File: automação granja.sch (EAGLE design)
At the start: 76 parts, among them IC1 MEGA8-P, IC10 A1322UA, IC11 A1322UA, IC12 A1322UA, IC2 MAX481CPA, IC3 A1322UA, IC4 A1322UA, IC5 78L05Z, IC7 A1322UA, IC8 A1322UA, IC9 A1322UA, K1 G2RA, K2 G2RA, K3 G2RA, K4 G2RA, K5 G2RA, K6 G2RA, K7 G2RA, K8 G2RA, Q1 BC548B, Q2 BC548B, Q3 BC548B, Q4 BC548B, Q6 BC548B, Q7 BC548B, Q8 BC548B, Q9 BC548B

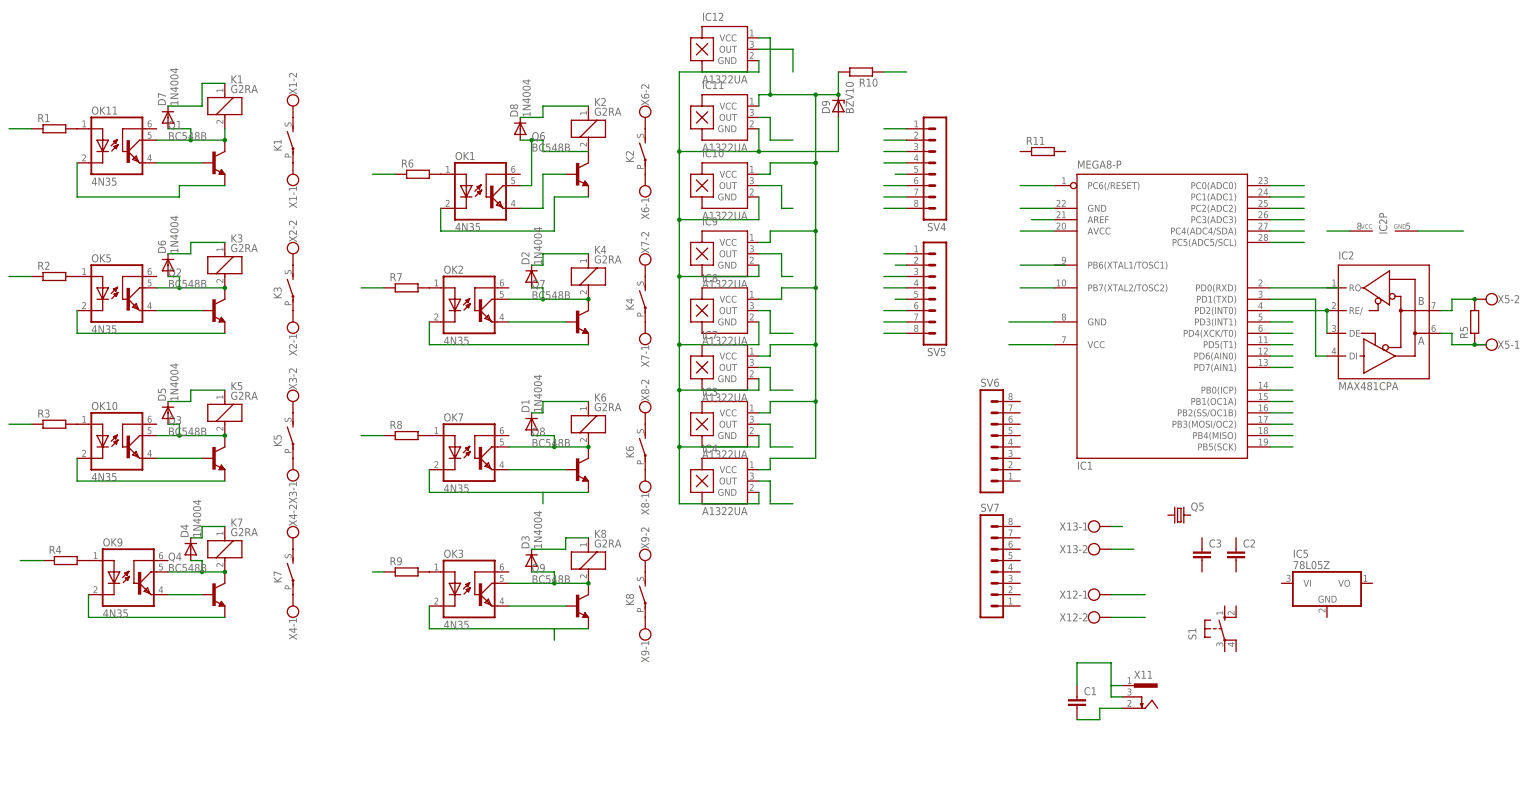
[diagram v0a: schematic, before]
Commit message: separadas controle de atuação e realimentação
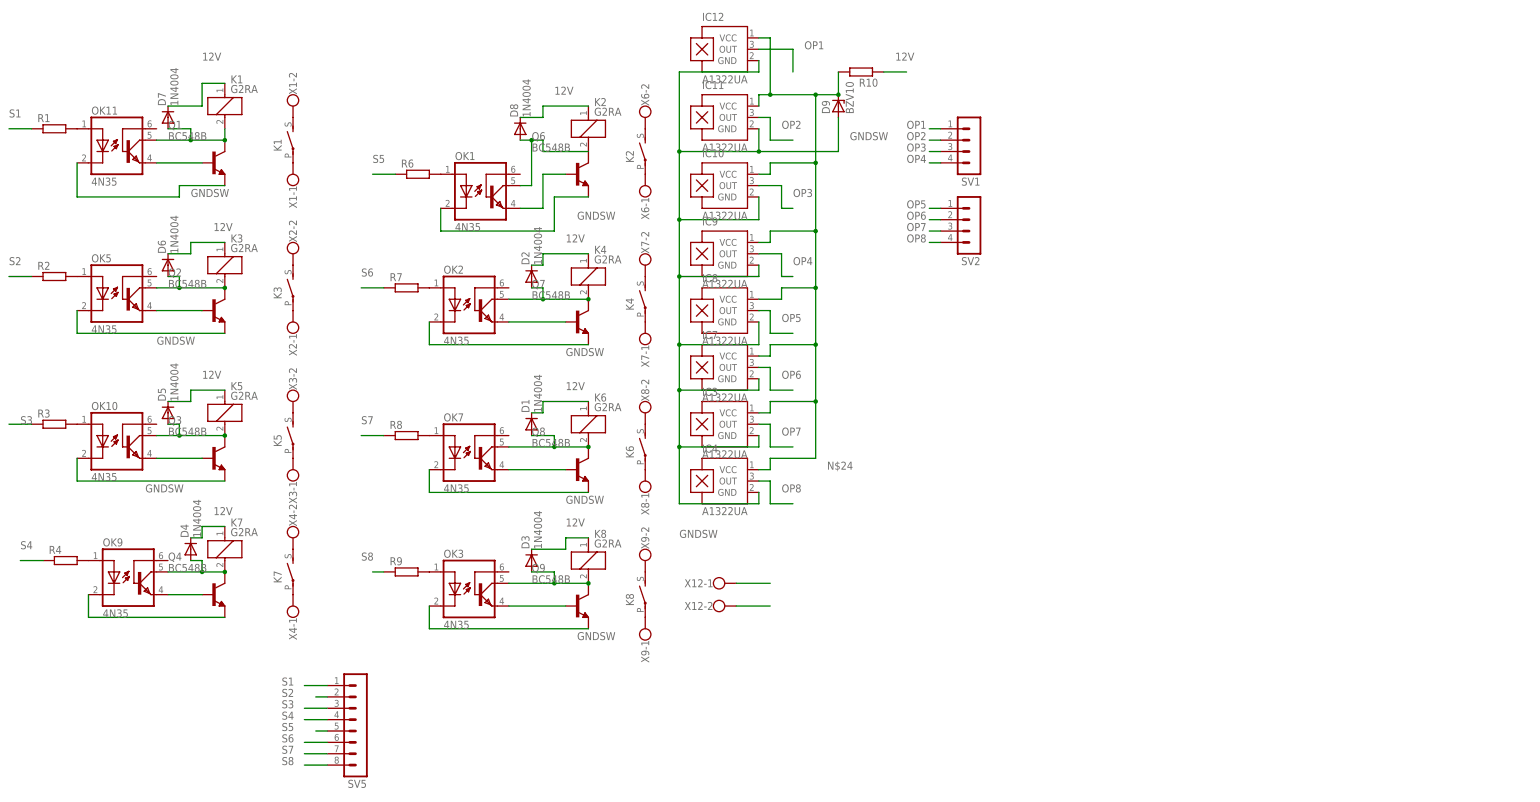
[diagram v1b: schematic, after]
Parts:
- removed C1, C2, C3: (no value), rcl:C-EU050-025X075
- removed IC1: MEGA8-P, atmel:MEGA8-P
- removed IC2: MAX481CPA, maxim:MAX481CPA
- removed IC5: 78L05Z, linear:78L05Z
- removed Q5: (no value), crystal:CRYSTALHC49U-V
- removed R11, R5: (no value), rcl:R-EU_0207/7
- removed S1: (no value), switch-omron:10-XX
- removed SV4, SV6, SV7: (no value), con-lstb:MA08-1
- removed X11: (no value), con-conrad:733980-62
- removed X13, X5: (no value), con-wago-500:W237-102
- added SV1, SV2: (no value), con-lstb:MA04-1
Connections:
- removed net 12VCTRL: C1.2, X11.2, X13-2.KL
- removed net GND: C1.1, IC1.AREF, IC1.GND@1, IC2P.GND, X11.1, X11.3, X13-1.KL
- removed net N$13: IC2G$1.B, R5.2, X5-2.KL
- removed net N$35: IC2G$1.A, R5.1, X5-1.KL
- removed net N$41: IC2P.VCC
- removed net N$42: IC1.VCC@1
- removed net N$43: IC1.PB7(XTAL2/TOSC2)
- removed net N$45: IC1.AVCC
- removed net N$46: IC1.GND
- removed net N$47: IC1.PC6(/RESET)
- removed net N$48: IC1.PC0(ADC0)
- removed net N$49: IC1.PC1(ADC1)
- removed net N$50: IC1.PC2(ADC2)
- removed net N$51: IC1.PC3(ADC3)
- removed net N$52: IC1.PC4(ADC4/SDA)
- removed net N$53: IC1.PC5(ADC5/SCL)
- removed net N$54: IC1.PD0(RXD)
- removed net N$55: IC1.PD1(TXD), IC2G$1.DI
- removed net N$56: IC1.PD2(INT0), IC2G$1.DE, IC2G$1.RE/
- removed net N$57: IC1.PD3(INT1)
- removed net N$58: IC1.PD4(XCK/T0)
- removed net N$59: IC1.PD5(T1)
- removed net N$60: IC1.PD6(AIN0)
- removed net N$61: IC1.PD7(AIN1)
- removed net N$62: IC1.PB0(ICP)
- removed net N$63: IC1.PB1(OC1A)
- removed net N$64: IC1.PB2(SS/OC1B)
- removed net N$65: IC1.PB3(MOSI/OC2)
- removed net N$66: IC1.PB4(MISO)
- removed net N$67: IC1.PB5(SCK)
- removed net N$84: D9.A, IC10.GND, IC11.GND, IC12.GND, IC3.GND, IC4.GND, IC7.GND, IC8.GND, IC9.GND
- net GNDSW: now also D9.A, IC10.GND, IC11.GND, IC12.GND, IC3.GND, IC4.GND, IC7.GND, IC8.GND, IC9.GND
- net OP1: now also SV1.1; no longer SV4.1
- net OP2: now also SV1.2; no longer SV4.2
- net OP3: now also SV1.3; no longer SV4.3
- net OP4: now also SV1.4; no longer SV4.4
- net OP5: now also SV2.1; no longer SV4.5
- net OP6: now also SV2.2; no longer SV4.6
- net OP7: now also SV2.3; no longer SV4.7
- net OP8: now also SV2.4; no longer SV4.8
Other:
- moved on the sheet: SV5, X12-1, X12-2
